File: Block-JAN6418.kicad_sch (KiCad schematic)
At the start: 17 parts, among them J1 B+, J2 Sig_gnd, J3 Sig_in, J4 Sig_out, J5 9V, U1 JAN6418, U2 LM317L

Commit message: narrow the board, and add some additional silkscreening
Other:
- moved on the sheet: J2, J5
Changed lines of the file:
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@@
 	(symbol
 		(lib_id "power:GND")
-		(at 29.21 24.13 0)
+		(at 20.32 40.64 0)
 		(unit 1)
 		(exclude_from_sim no)
@@
 		(fields_autoplaced yes)
 		(property "Reference" "#PWR05"
-			(at 29.21 30.48 0)
+			(at 20.32 46.99 0)
 			(effects
 				(font
@@
 		)
 		(property "Value" "GND"
-			(at 29.21 29.21 0)
+			(at 20.32 45.72 0)
 			(effects
 				(font
@@
 		)
 		(property "Footprint" ""
-			(at 29.21 24.13 0)
+			(at 20.32 40.64 0)
 			(effects
 				(font
@@
 		)
 		(property "Datasheet" ""
-			(at 29.21 24.13 0)
+			(at 20.32 40.64 0)
 			(effects
 				(font
@@
 		)
 		(property "Description" "Power symbol creates a global label with name \"GND\" , ground"
-			(at 29.21 24.13 0)
+			(at 20.32 40.64 0)
 			(effects
 				(font
@@
 	(symbol
 		(lib_id "power:+9V")
-		(at 26.67 39.37 0)
+		(at 25.4 24.13 0)
 		(unit 1)
 		(exclude_from_sim no)
@@
 		(fields_autoplaced yes)
 		(property "Reference" "#PWR06"
-			(at 26.67 43.18 0)
+			(at 25.4 27.94 0)
 			(effects
 				(font
@@
 		)
 		(property "Value" "+9V"
-			(at 26.67 34.29 0)
+			(at 25.4 19.05 0)
 			(effects
 				(font
@@
 		)
 		(property "Footprint" ""
-			(at 26.67 39.37 0)
+			(at 25.4 24.13 0)
 			(effects
 				(font
@@
 		)
 		(property "Datasheet" ""
-			(at 26.67 39.37 0)
+			(at 25.4 24.13 0)
 			(effects
 				(font
@@
 		)
 		(property "Description" "Power symbol creates a global label with name \"+9V\""
-			(at 26.67 39.37 0)
+			(at 25.4 24.13 0)
 			(effects
 				(font
@@
 	(symbol
 		(lib_id "Connector:Screw_Terminal_01x01")
-		(at 21.59 39.37 180)
+		(at 20.32 24.13 180)
 		(unit 1)
 		(exclude_from_sim no)
@@
 		(fields_autoplaced yes)
 		(property "Reference" "J5"
-			(at 21.59 33.02 0)
+			(at 20.32 17.78 0)
 			(effects
 				(font
@@
 		)
 		(property "Value" "9V"
-			(at 21.59 35.56 0)
+			(at 20.32 20.32 0)
 			(effects
 				(font
@@
 		)
 		(property "Footprint" "TerminalBlock_MetzConnect:TerminalBlock_MetzConnect_360271_1x01_Horizontal_ScrewM3.0_Boxed"
-			(at 21.59 39.37 0)
+			(at 20.32 24.13 0)
 			(effects
 				(font
@@
 		)
 		(property "Datasheet" "~"
-			(at 21.59 39.37 0)
+			(at 20.32 24.13 0)
 			(effects
 				(font
@@
 		)
 		(property "Description" "Generic screw terminal, single row, 01x01, script generated (kicad-library-utils/schlib/autogen/connector/)"
-			(at 21.59 39.37 0)
+			(at 20.32 24.13 0)
 			(effects
 				(font
@@
 	(symbol
 		(lib_id "Connector:Screw_Terminal_01x01")
-		(at 29.21 19.05 90)
+		(at 20.32 35.56 90)
 		(unit 1)
 		(exclude_from_sim no)
@@
 		(fields_autoplaced yes)
 		(property "Reference" "J2"
-			(at 31.75 17.7799 90)
+			(at 22.86 34.2899 90)
 			(effects
 				(font
@@
 		)
 		(property "Value" "Sig_gnd"
-			(at 31.75 20.3199 90)
+			(at 22.86 36.8299 90)
 			(effects
 				(font
@@
 		)
 		(property "Footprint" "TerminalBlock_MetzConnect:TerminalBlock_MetzConnect_360271_1x01_Horizontal_ScrewM3.0_Boxed"
-			(at 29.21 19.05 0)
+			(at 20.32 35.56 0)
 			(effects
 				(font
@@
 		)
 		(property "Datasheet" "~"
-			(at 29.21 19.05 0)
+			(at 20.32 35.56 0)
 			(effects
 				(font
@@
 		)
 		(property "Description" "Generic screw terminal, single row, 01x01, script generated (kicad-library-utils/schlib/autogen/connector/)"
-			(at 29.21 19.05 0)
-			(effects
-				(font
+			(at 20.32 35.56 0)
+			(effects
+				(font

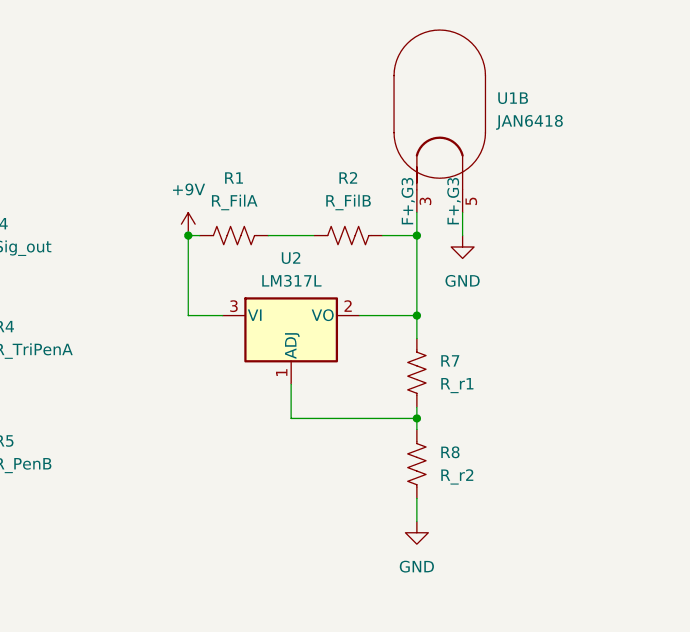
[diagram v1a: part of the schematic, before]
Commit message: bigger change...
1. Added L1 Ground Plane
2. Added filter and bandpass capacitors to LM317L optional block
3. `Sig_in` and `Sig_gnd` swapped physical locations...
    1. `Sig_gnd` is now closer to PSU block ground connections (lower
       impedance ground paths)
    2. `Sig_gnd` now closer to `R_impedance` ground connection
    3. `Sig_gnd` distance to `JAN6418` ground pin is about unchanged
4. Other general changes and general notes
    1. Valve heater power now routed further away from valve body
    2. Power blocks now a bit more compact, and further away from valve
       body
    3. No impeded ground paths on the ground plane (e.g. no going around
       vias, pins, etc; all straight line paths to `Sig_gnd`)
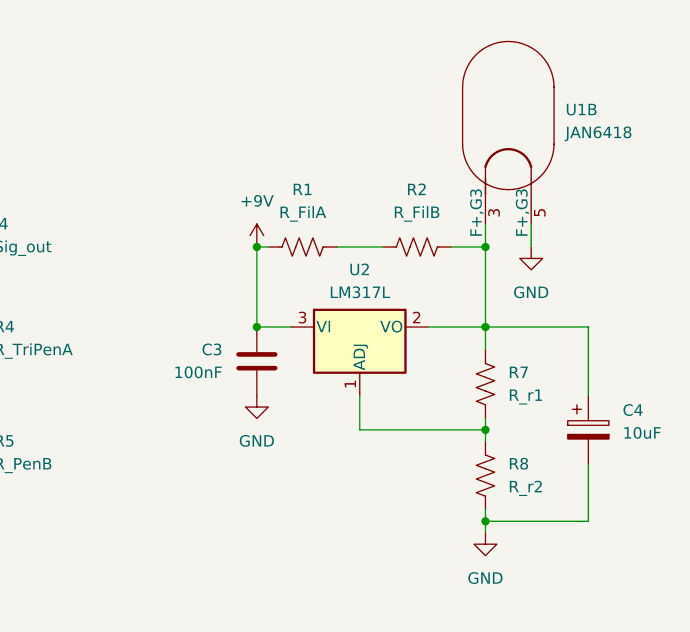
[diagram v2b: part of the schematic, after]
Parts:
- added C3: 100nF, Capacitor_THT:C_Rect_L4.6mm_W2.0mm_P2.50mm_MKS02_FKP02, symbol Device:C
- added C4: 10uF, Capacitor_THT:CP_Radial_Tantal_D4.5mm_P5.00mm, symbol Device:C_Polarized
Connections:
- net +9V: now also C3.1
- net GND: now also C3.2, C4.2
- net at R2.2, R7.2, U1.3 (F+,G3)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: now also C4.1
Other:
- moved on the sheet: R1, R2, R7, R8, U1B, U2

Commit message: update sch from pcb, gen gerbers, drl files
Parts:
- C4: value 10uF -> 1uF; footprint Capacitor_THT:CP_Radial_Tantal_D4.5mm_P5.00mm -> Capacitor_THT:CP_Radial_D4.0mm_P1.50mm
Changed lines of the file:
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@@
 			)
 		)
-		(property "Value" "10uF"
+		(property "Value" "1uF"
 			(at 140.97 62.6109 0)
 			(effects
@@
 			)
 		)
-		(property "Footprint" "Capacitor_THT:CP_Radial_Tantal_D4.5mm_P5.00mm"
+		(property "Footprint" "Capacitor_THT:CP_Radial_D4.0mm_P1.50mm"
 			(at 138.1252 66.04 0)
 			(effects

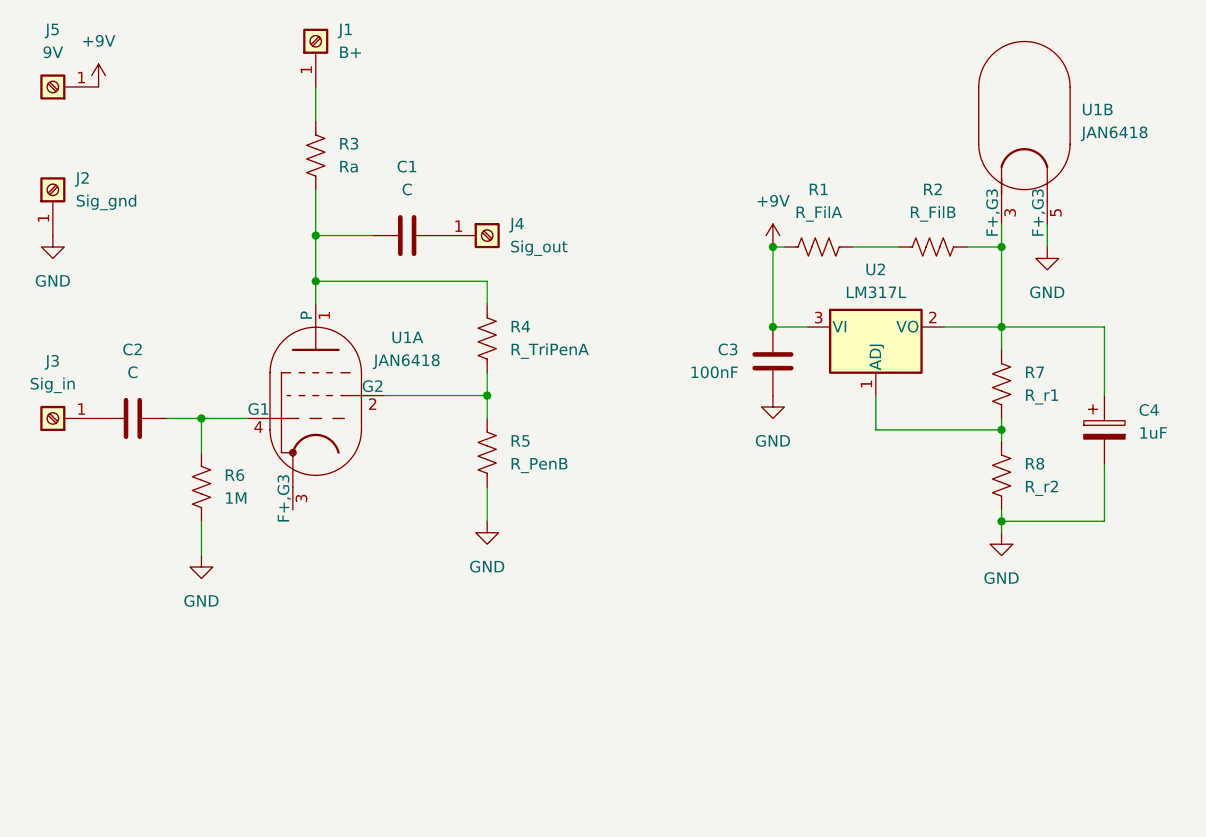
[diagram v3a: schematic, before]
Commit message: v1.0b Re-routing
- Added ground fill to L2, respective vias
- Re-routed power rail solder points to the bottom of the board so that
  power can be jumpered up from the enclosure front board (will house
  power bars, I/O, pots, etc)
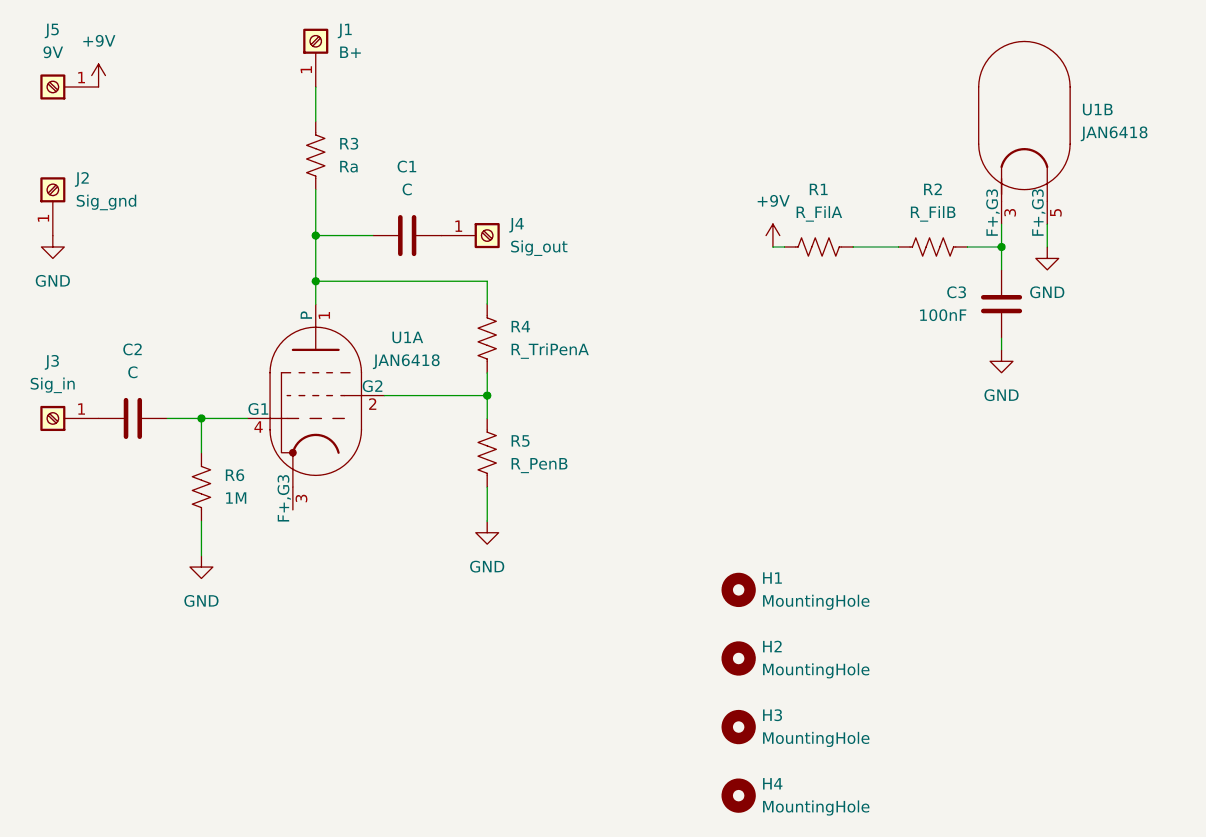
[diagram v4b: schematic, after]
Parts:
- removed C4: 1uF, Capacitor_THT:CP_Radial_D4.0mm_P1.50mm, symbol Device:C_Polarized
- removed R7: R_r1, Resistor_THT:R_Axial_DIN0207_L6.3mm_D2.5mm_P2.54mm_Vertical, symbol Device:R_US
- removed R8: R_r2, Resistor_THT:R_Axial_DIN0207_L6.3mm_D2.5mm_P2.54mm_Vertical, symbol Device:R_US
- removed U2: LM317L, Package_TO_SOT_THT:TO-92_Inline_Wide, symbol Regulator_Linear:LM317L_TO92
- added H1, H2, H3, H4: MountingHole, MountingHole:MountingHole_2.2mm_M2, symbol Mechanical:MountingHole
- R1, R2: footprint Resistor_THT:R_Axial_DIN0207_L6.3mm_D2.5mm_P2.54mm_Vertical -> Resistor_THT:R_Axial_DIN0309_L9.0mm_D3.2mm_P2.54mm_Vertical
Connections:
- net +9V: no longer C3.1
- net at R2.2, U1.3 (F+,G3): now also C3.1
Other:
- moved on the sheet: C3

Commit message: tighten up some alignments
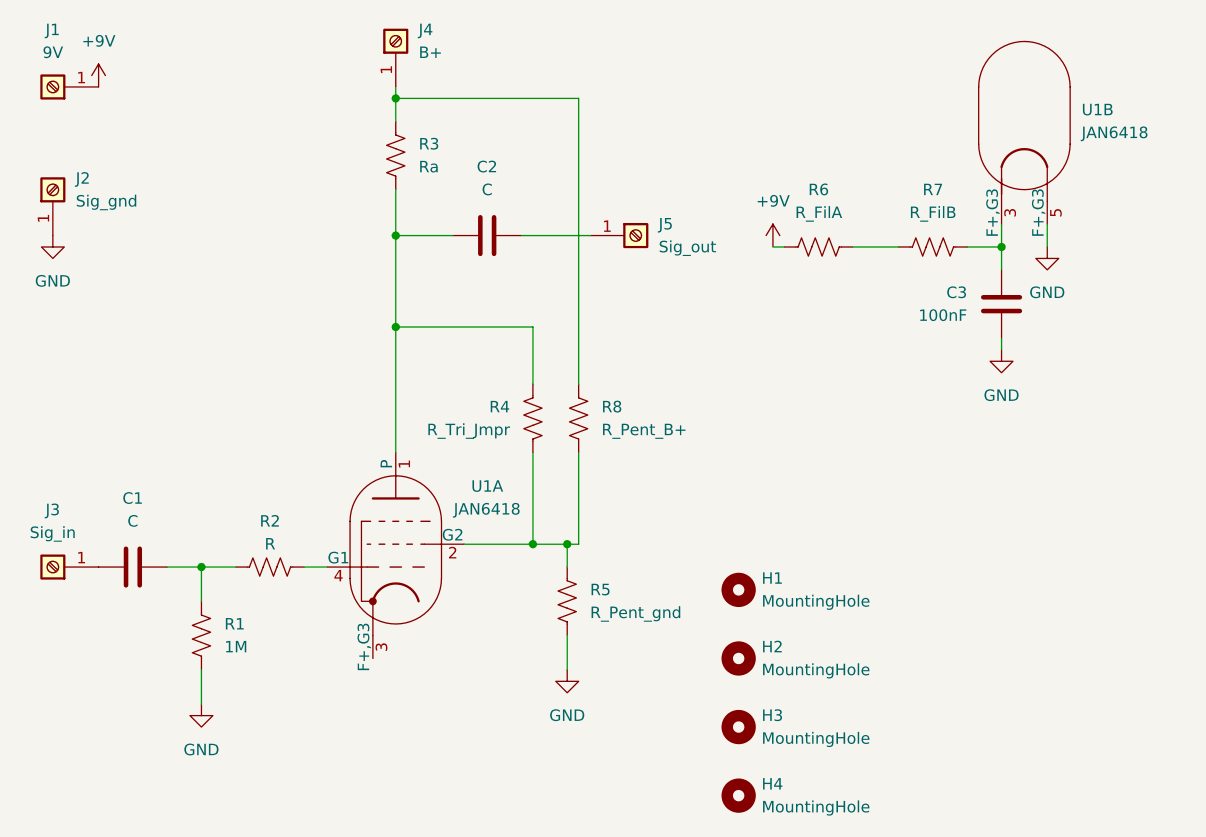
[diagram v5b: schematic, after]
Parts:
- added R2: R, Resistor_THT:R_Axial_DIN0309_L9.0mm_D3.2mm_P12.70mm_Horizontal, symbol Device:R_US
- added R8: R_Pent_B+, Resistor_THT:R_Axial_DIN0309_L9.0mm_D3.2mm_P2.54mm_Vertical, symbol Device:R_US
- R4: value R_TriPenA -> R_Tri_Jmpr
- R5: value R_PenB -> R_Pent_gnd
- renumbered C2 to C1, C1 to C2, J5 to J1, J1 to J4, J4 to J5, R6 to R1, R1 to R6, R2 to R7
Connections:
- net at R4.2, R5.1, U1.2 (G2): now also R8.2
- net at J4.1 (Pin_1), R3.1: now also R8.1
- net at C1.2, R1.1: now also R2.1; no longer U1.4 (G1)
- new net: R2.2, U1.4 (G1)
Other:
- moved on the sheet: C1, C2, J3, J4, J5, R1, R3, R4, R5, U1A
